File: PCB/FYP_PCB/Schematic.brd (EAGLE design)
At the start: 100 x 100 mm, 18 parts, among them IC1 7805TV

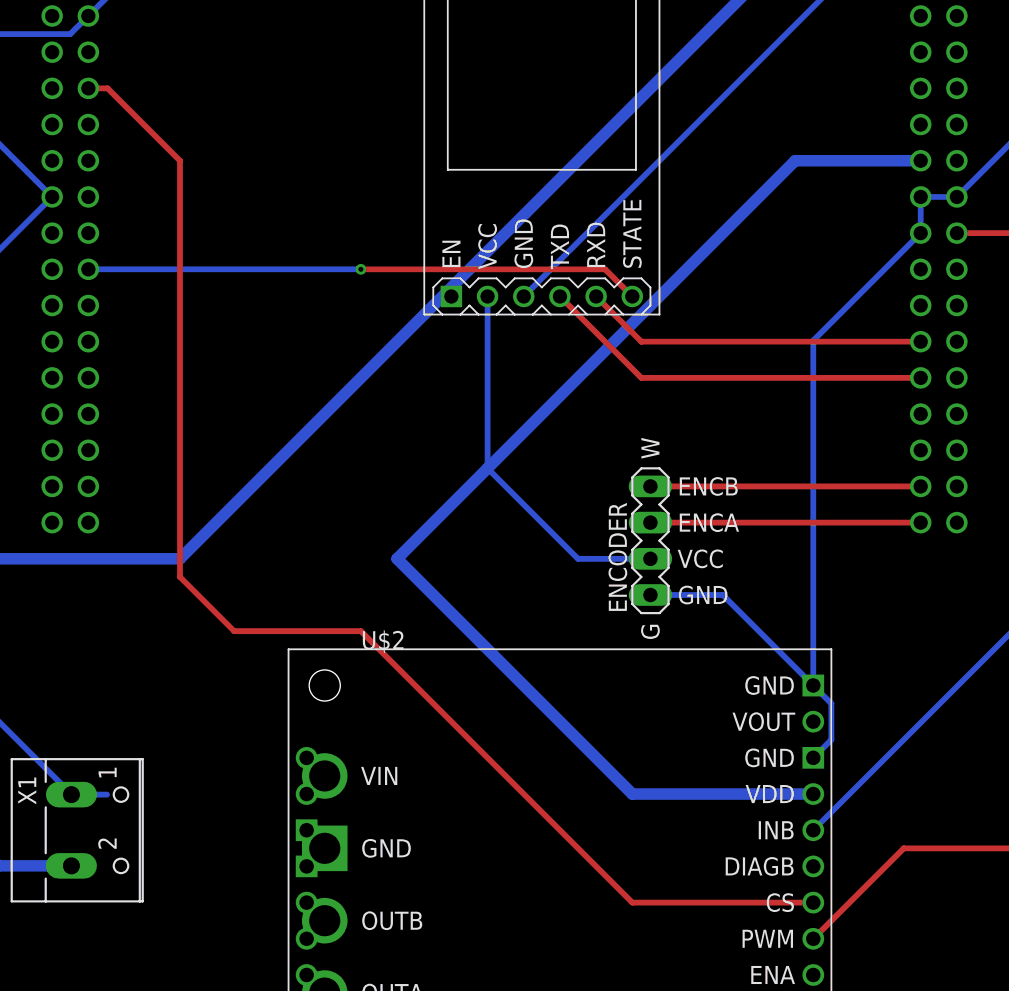
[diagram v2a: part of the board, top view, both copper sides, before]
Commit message: Update PCB to put CS on an ADC pin.
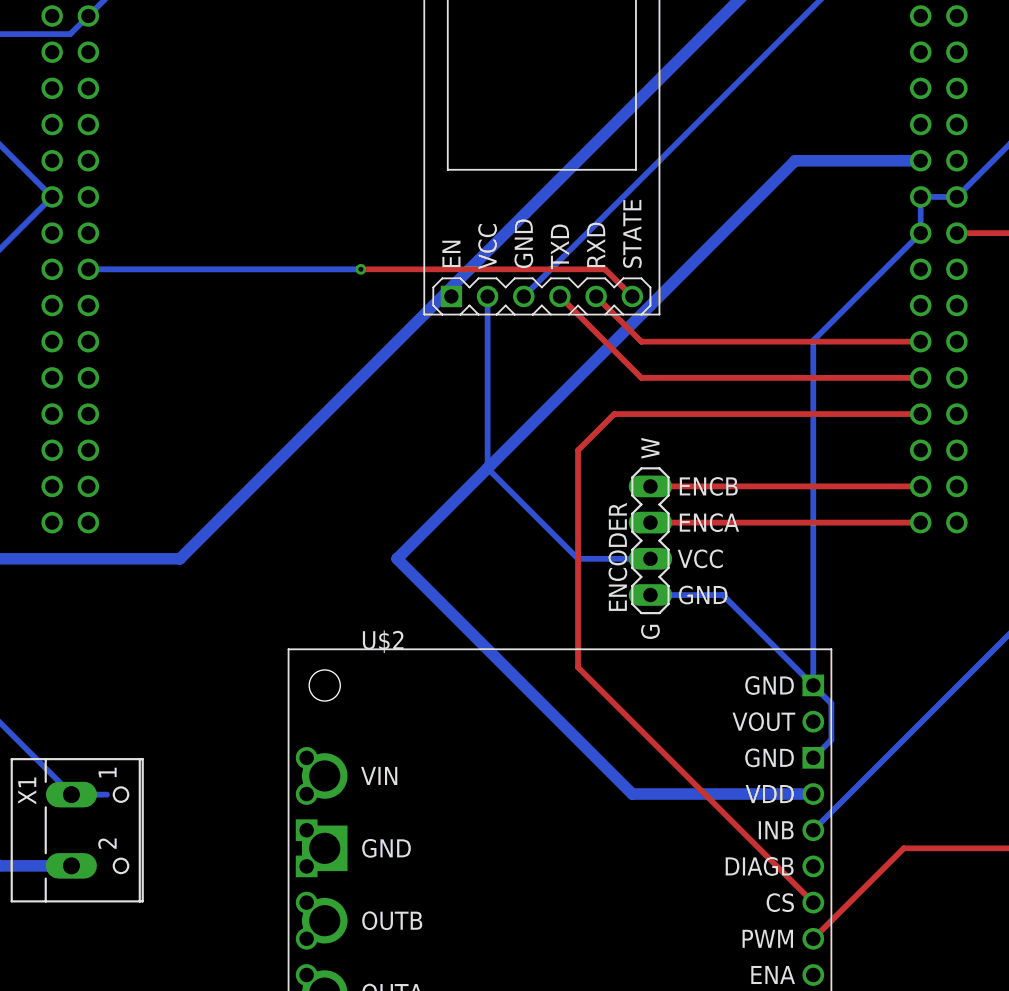
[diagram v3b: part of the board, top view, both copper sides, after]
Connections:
- removed net N$3: U$1.CN10_13, U$2.CS
- new net N$13: U$1.CN7_32, U$2.CS
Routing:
- net N$3: track 91.7 -> 0.00 mm
- net N$13: track 0.00 -> 63.7 mm
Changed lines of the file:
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@@
 <wire x1="91.44" y1="59.69" x2="81.2" y2="59.69" width="0.4064" layer="1"/>
-</signal>
-<signal name="N$3">
-<contactref element="U$1" pad="CN10_13"/>
-<contactref element="U$2" pad="CS"/>
-<wire x1="71.12" y1="12.7" x2="58.42" y2="12.7" width="0.4064" layer="1"/>
-<wire x1="39.37" y1="31.75" x2="30.48" y2="31.75" width="0.4064" layer="1"/>
-<wire x1="30.48" y1="31.75" x2="26.67" y2="35.56" width="0.4064" layer="1"/>
-<wire x1="26.67" y1="35.56" x2="26.67" y2="64.77" width="0.4064" layer="1"/>
-<wire x1="26.67" y1="64.77" x2="21.59" y2="69.85" width="0.4064" layer="1"/>
-<wire x1="21.59" y1="69.85" x2="20.24" y2="69.85" width="0.4064" layer="1"/>
-<wire x1="58.42" y1="12.7" x2="39.37" y2="31.75" width="0.4064" layer="1"/>
 </signal>
 <signal name="N$4">
@@
 <wire x1="59.69" y1="39.37" x2="78.66" y2="39.37" width="0.4064" layer="1"/>
 </signal>
+<signal name="N$13">
+<contactref element="U$2" pad="CS"/>
+<contactref element="U$1" pad="CN7_32"/>
+<wire x1="71.12" y1="12.7" x2="54.61" y2="29.21" width="0.4064" layer="1"/>
+<wire x1="54.61" y1="29.21" x2="54.61" y2="44.45" width="0.4064" layer="1"/>
+<wire x1="54.61" y1="44.45" x2="57.15" y2="46.99" width="0.4064" layer="1"/>
+<wire x1="57.15" y1="46.99" x2="78.66" y2="46.99" width="0.4064" layer="1"/>
+</signal>
 </signals>

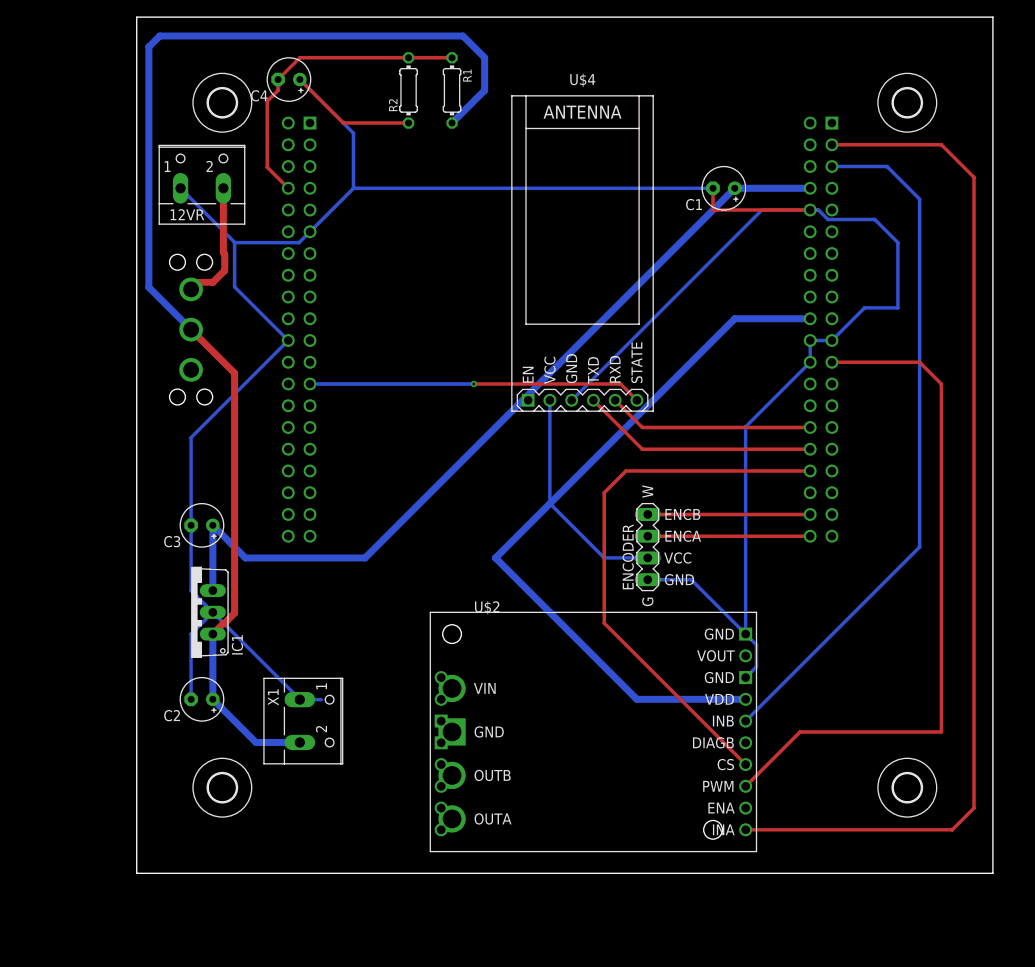
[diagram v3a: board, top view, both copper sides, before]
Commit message: Change PCB layout and generate gerber files for production.
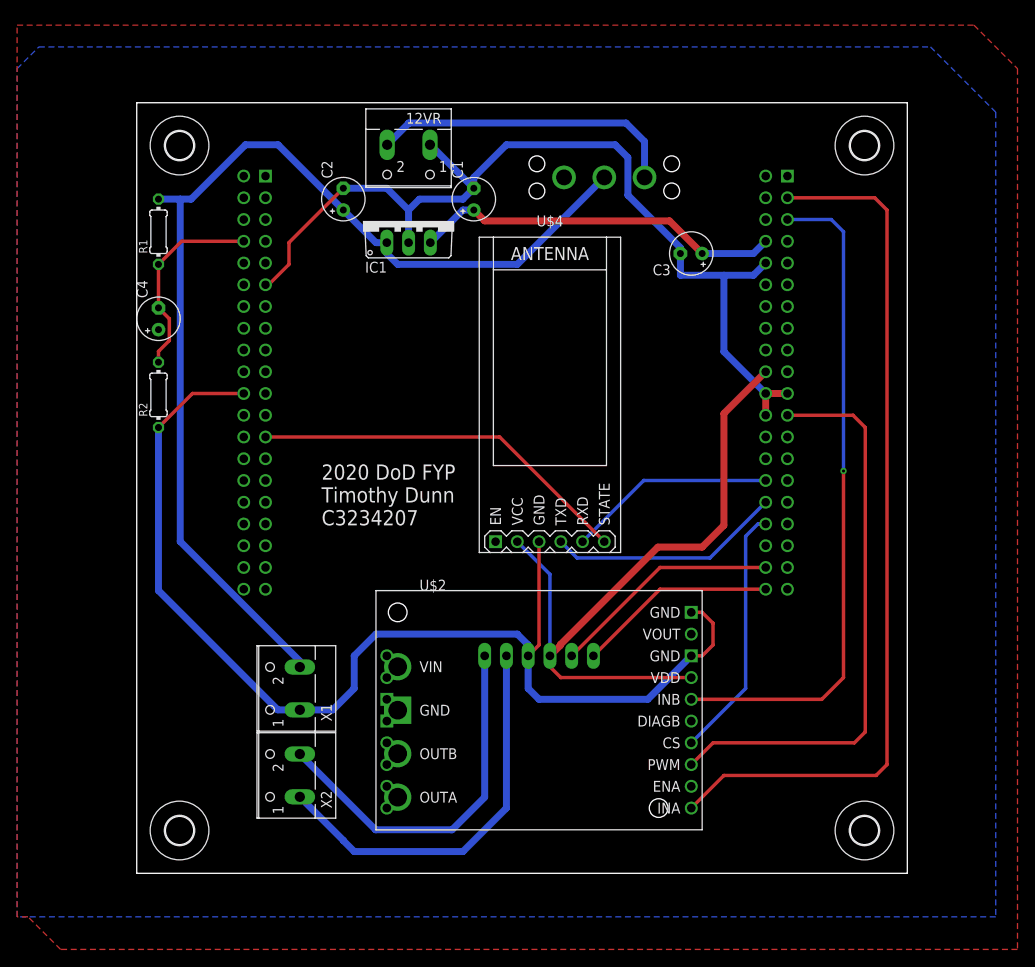
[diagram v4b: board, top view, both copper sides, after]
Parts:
- removed ENCODER: (no value), Custom:MA04-1
- added SV1: (no value), Custom:MA06-1
- added X2: (no value), con-wago-500:W237-102
- moved H4 85.1 mm to (5.00, 85.0)
- moved H2 75.2 mm to (85.0, 85.0)
- moved C3 65.4 mm to (64.8, 72.4)
- moved C2 60.7 mm to (24.1, 78.7), turned to 90 degrees
- moved IC1 52.3 mm to (31.8, 76.2), turned to 0 degrees
- moved U$3 51.4 mm to (54.6, 81.3), turned to 90 degrees
- moved R2 46.0 mm to (2.54, 55.9)
- moved R1 38.1 mm to (2.54, 74.9), turned to 90 degrees
- moved C4 31.8 mm to (2.54, 64.8), turned to 90 degrees
- moved C1 29.2 mm to (39.4, 78.7), turned to 90 degrees
- moved 12VR 24.3 mm to (31.8, 83.8), turned to 180 degrees
- moved U$4 16.9 mm to (48.3, 55.9)
- moved U$1 8.08 mm to (44.5, 55.9)
- moved H1 7.07 mm to (5.00, 5.00), turned to 0 degrees
- moved H3 7.07 mm to (85.0, 5.00)
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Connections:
- new net N$14: SV1.MTRPWR+, X2.2
- new net N$3: SV1.MTRPWR-, X2.1
- net GND: now also SV1.ENCGND; no longer ENCODER.GND
- net N$5: now also SV1.ENCVCC; no longer ENCODER.VCC
- net N$6: now also SV1.ENCA; no longer ENCODER.ENCB
- net N$7: now also SV1.ENCB; no longer ENCODER.ENCA
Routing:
- net GND: track 317.0 -> 248.2 mm
- net N$10: track 96.9 -> 43.4 mm
- net N$3: track 0.00 -> 46.7 mm
- net N$14: track 0.00 -> 43.3 mm
- net N$13: track 63.7 -> 29.7 mm
- net N$5: track 111.8 -> 79.9 mm
- net N$8: track 14.5 -> 36.2 mm
- net +12V: track 143.7 -> 125.9 mm
- net N$1: track 119.6 -> 102.0 mm
- net N$2: track 80.0 -> 67.1 mm
- net N$15: track 35.6 -> 23.6 mm
- net N$6: track 19.0 -> 26.9 mm
- net N$12: track 39.0 -> 44.6 mm, vias 1 -> 0
- net N$7: track 19.0 -> 23.3 mm
- net N$4: track 81.2 -> 78.0 mm, vias 0 -> 1
- added copper zone on layer 1, net GND
- added copper zone on layer 16, net GND
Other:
- board size 100 x 100 mm -> 90 x 90 mm
- board text added: "2020 DoD FYP Timothy Dunn C3234207"
- board text added: "STM32 GOES HERE ^^^^USB UP^^^^"
